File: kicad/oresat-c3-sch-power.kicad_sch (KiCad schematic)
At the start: 67 parts, among them U31 LP2985AIM5-3.3, U34 TPS259621DDA, U35 TPS259620DDA, U36 LTC3624-5, U38 LP2985AIM5-3.3, U6 LTC3624-5

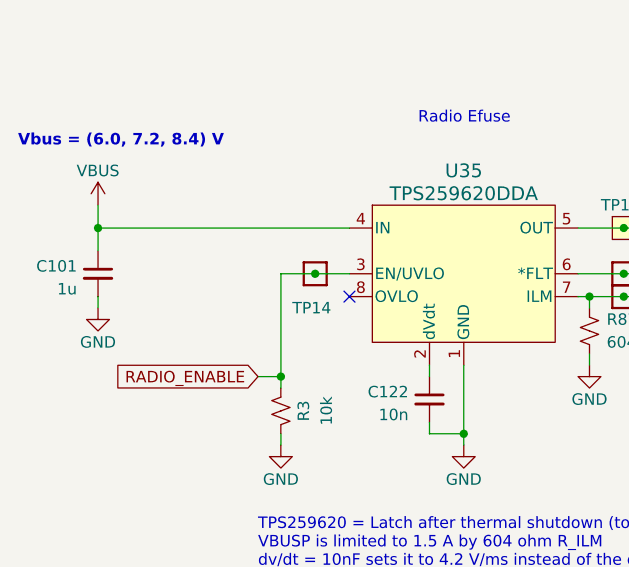
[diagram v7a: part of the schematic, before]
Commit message: Fixed some issues, including adding mrore capacitance. Also switched back to 0.38 mm for 50 ohm lines.
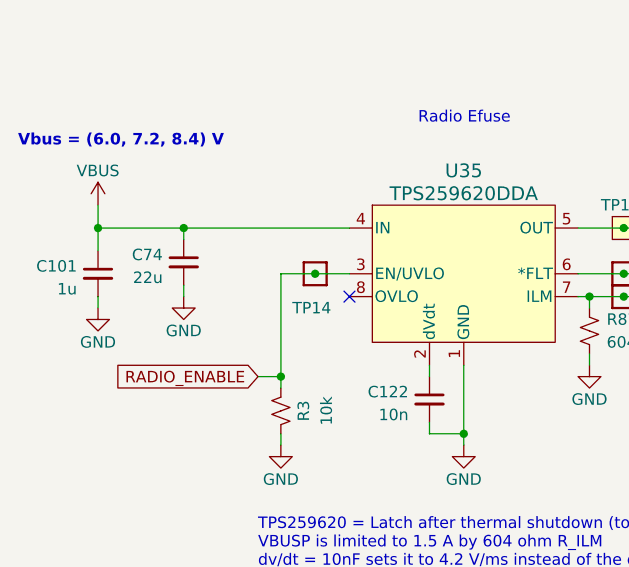
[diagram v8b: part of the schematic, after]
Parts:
- added C74: 22u, Capacitor_SMD:C_1210_3225Metric, symbol Device:C_Small
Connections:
- net GND: now also C74.2
- net VBUS: now also C74.1
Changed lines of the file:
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@@
   (junction (at 230.505 80.01) (diameter 0) (color 0 0 0 0)
+  )
+  (junction (at 64.77 152.4) (diameter 0) (color 0 0 0 0)
   )
   (junction (at 161.925 152.4) (diameter 0) (color 0 0 0 0)
@@
     (stroke (width 0) (type default))
   )
+  (wire (pts (xy 64.77 158.75) (xy 64.77 160.02))
+    (stroke (width 0) (type default))
+  )
   (wire (pts (xy 327.66 167.64) (xy 327.66 166.37))
     (stroke (width 0) (type default))
@@
     (stroke (width 0) (type default))
   )
+  (wire (pts (xy 64.77 152.4) (xy 83.185 152.4))
+    (stroke (width 0) (type default))
+  )
   (wire (pts (xy 349.25 186.69) (xy 349.25 187.96))
     (stroke (width 0) (type default))
@@
     (stroke (width 0) (type default))
   )
-  (wire (pts (xy 55.245 152.4) (xy 83.185 152.4))
+  (wire (pts (xy 55.245 152.4) (xy 64.77 152.4))
     (stroke (width 0) (type default))
   )
@@
   )
   (wire (pts (xy 135.255 80.01) (xy 123.825 80.01))
+    (stroke (width 0) (type default))
+  )
+  (wire (pts (xy 64.77 152.4) (xy 64.77 153.67))
     (stroke (width 0) (type default))
   )
@@
     )
   )
+  (symbol (lib_id "power:GND") (at 64.77 160.02 0) (unit 1)
+    (in_bom yes) (on_board yes) (dnp no)
+    (property "Reference" "#PWR016" (at 64.77 166.37 0)
+      (effects (font (size 1.27 1.27)) hide)
+    )
+    (property "Value" "GND" (at 64.77 163.83 0)
+      (effects (font (size 1.27 1.27)))
+    )
+    (property "Footprint" "" (at 64.77 160.02 0)
+      (effects (font (size 1.27 1.27)) hide)
+    )
+    (property "Datasheet" "" (at 64.77 160.02 0)
+      (effects (font (size 1.27 1.27)) hide)
+    )
+    (pin "1")
+    (instances
+      (project "oresat-c3"
+        (path "/65d12cdd-c326-4033-9053-c59fa4e0b25e/2134bb9a-062c-4e32-a41e-d15ce3545372"
+          (reference "#PWR016") (unit 1)
+        )
+      )
+    )
+  )
   (symbol (lib_id "oresat-misc:Test-Point-0.75mm-th") (at 272.415 72.39 0) (unit 1)
     (in_bom yes) (on_board yes) (dnp no)
@@
         )
       )
+    )
+  )
+  (symbol (lib_id "Device:C_Small") (at 64.77 156.21 0) (mirror y) (unit 1)
+    (in_bom yes) (on_board yes) (dnp no)
+    (property "Reference" "C74" (at 62.4459 155.3816 0)
+      (effects (font (size 1.27 1.27)) (justify left))
+    )
+    (property "Value" "22u" (at 62.4459 157.9185 0)
+      (effects (font (size 1.27 1.27)) (justify left))
+    )
+    (property "Footprint" "Capacitor_SMD:C_1210_3225Metric" (at 64.77 156.21 0)
+      (effects (font (size 1.27 1.27)) hide)
+    )
+    (property "Datasheet" "~" (at 64.77 156.21 0)
+      (effects (font (size 1.27 1.27)) hide)
+    )
+    (property "Description" "CAP CER 22UF 16V X7R 1210" (at 64.77 156.21 0)
+      (effects (font (size 1.27 1.27)) hide)
+    )
+    (property "MFR" "Samsung Electro-Mechanics" (at 64.77 156.21 0)
+      (effects (font (size 1.27 1.27)) hide)
+    )
+    (property "MPN" "CL32B226MOJVPNE" (at 64.77 156.21 0)
+      (effects (font (size 1.27 1.27)) hide)
+    )
+    (pin "1")
+    (pin "2")
+    (instances
+      (project "oresat-c3"
+        (path "/65d12cdd-c326-4033-9053-c59fa4e0b25e/2134bb9a-062c-4e32-a41e-d15ce3545372"
+          (reference "C74") (unit 1)
+        )
+      )
